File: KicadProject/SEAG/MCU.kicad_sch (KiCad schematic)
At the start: 11 parts, among them IC1 STM32F722RCT6, SW1 SW_SPDT, Y1 Crystal_GND24

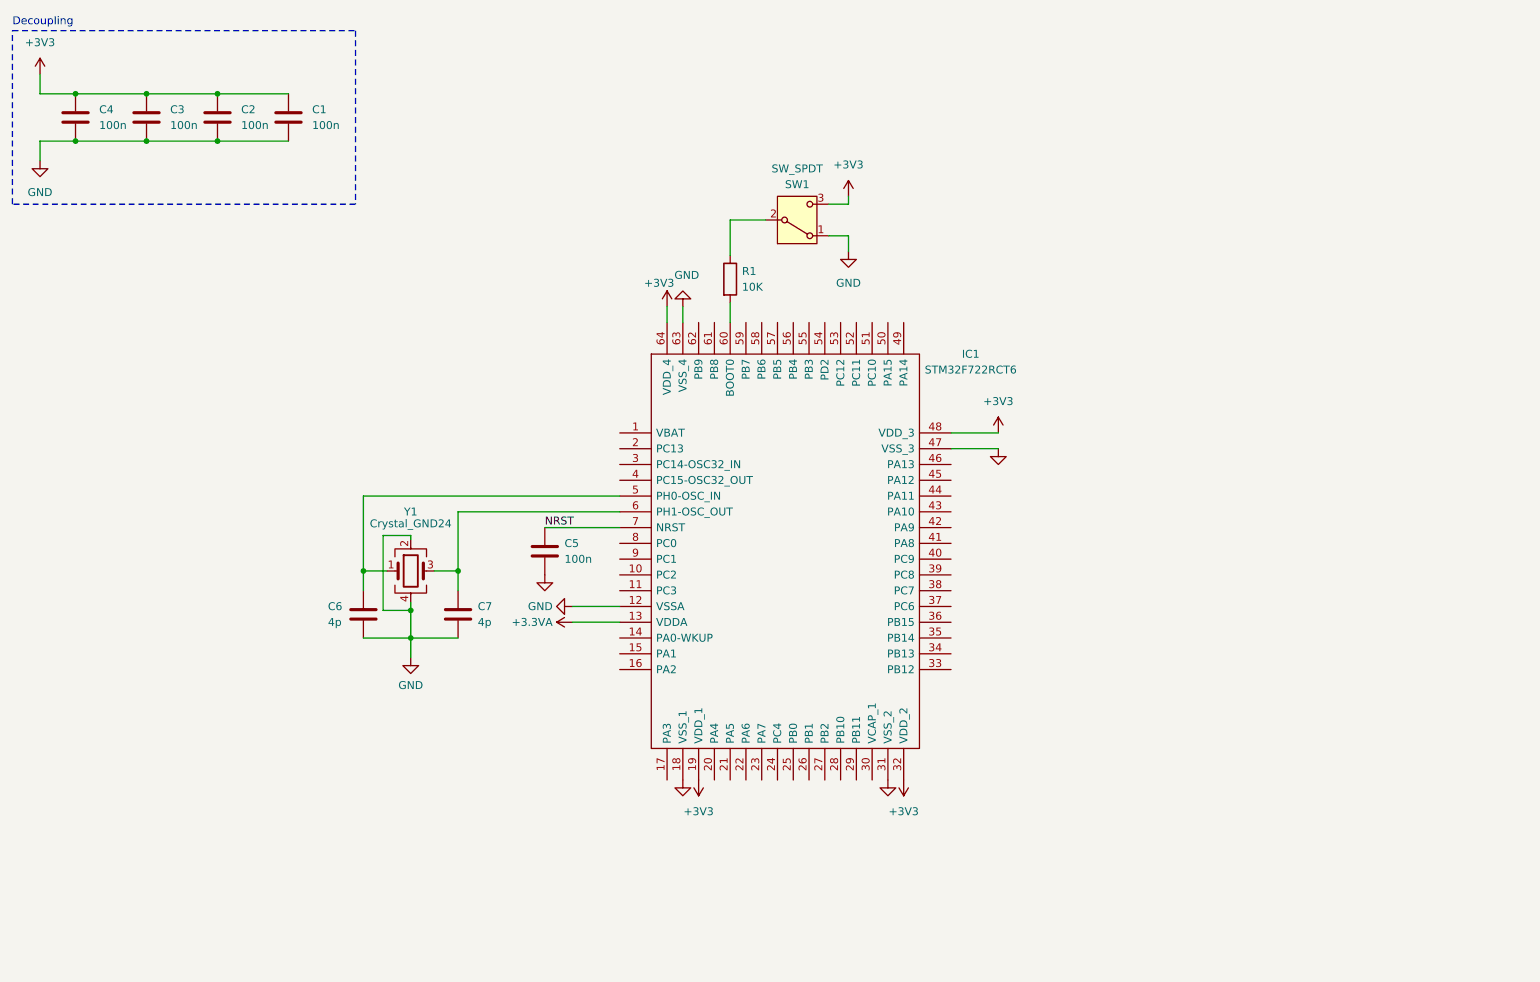
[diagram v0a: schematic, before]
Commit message: Added power supply and serial link header to PCB schematic
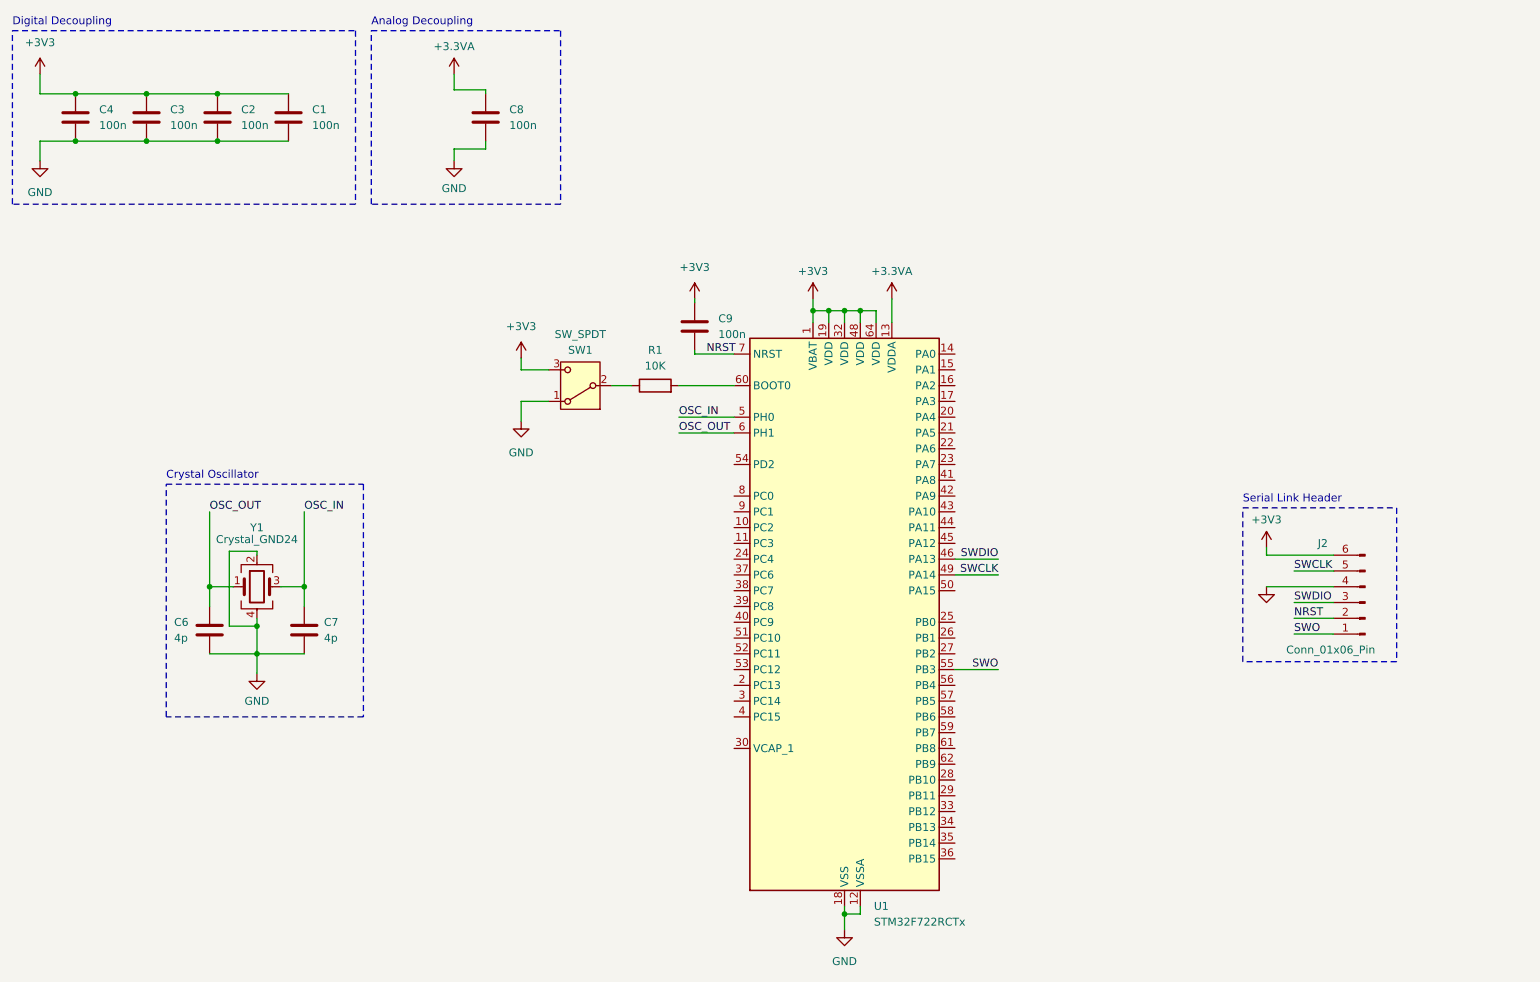
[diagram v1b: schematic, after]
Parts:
- removed C5: 100n, symbol Device:C
- removed IC1: STM32F722RCT6, QFP50P1200X1200X160-64N, symbol SamacSys_Parts:STM32F722RCT6
- added C8, C9: 100n, symbol Device:C
- added J2: Conn_01x06_Pin, Connector_PinHeader_2.54mm:PinHeader_1x06_P2.54mm_Vertical, symbol Connector:Conn_01x06_Pin
- added U1: STM32F722RCTx, Package_QFP:LQFP-64_10x10mm_P0.5mm, symbol MCU_ST_STM32F7:STM32F722RCTx
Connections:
- net +3.3VA: now also C8.1, U1.13 (VDDA)
- net +3V3: now also C9.1, J2.6 (Pin_6), U1.1 (VBAT), U1.19 (VDD), U1.32 (VDD), U1.48 (VDD), U1.64 (VDD)
- net GND: now also C8.2, J2.4 (Pin_4), U1.12 (VSSA), U1.18 (VSS), U1.31 (VSS), U1.47 (VSS), U1.63 (VSS)
- net NRST: now also C9.2, J2.2 (Pin_2), U1.7 (NRST)
- net OSC_IN: now reaches C7.1, Y1.3
- net OSC_IN: now also U1.5 (PH0)
- net at R1.2: now also U1.60 (BOOT0)
- net OSC_OUT: now reaches C6.1, Y1.1
- net OSC_OUT: now also U1.6 (PH1)
- new net SWCLK: J2.5 (Pin_5), U1.49 (PA14)
- new net SWDIO: J2.3 (Pin_3), U1.46 (PA13)
- new net SWO: J2.1 (Pin_1), U1.55 (PB3)
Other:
- note added: "Analog Decoupling"
- note added: "Crystal Oscillator"
- note added: "Digital Decoupling"
- note added: "Serial Link Header"
- note removed: "Decoupling"
- title: (none) -> MCU
- moved on the sheet: C6, C7, R1, SW1, Y1

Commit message: Added 'AudioFiltering' and 'Codec' sheets to PCB schematic, started PCB layout with decouple caps and MCU. The codec in sheet 'Codec' is wrong, placed for testing
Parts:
- C1, C2, C3, C4, C6, C7, C8: footprint (none) -> Capacitor_SMD:C_0805_2012Metric
- C13: renamed from C9; footprint (none) -> Capacitor_SMD:C_0805_2012Metric
- R1: footprint (none) -> Resistor_SMD:R_0805_2012Metric
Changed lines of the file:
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@@
       (effects (font (size 1.27 1.27)) (justify left))
     )
-    (property "Footprint" "" (at 68.9102 120.65 0)
+    (property "Footprint" "Capacitor_SMD:C_0805_2012Metric" (at 68.9102 120.65 0)
       (effects (font (size 1.27 1.27)) hide)
     )
@@
       (effects (font (size 1.27 1.27)) (justify left))
     )
-    (property "Footprint" "" (at 66.3702 38.1 0)
+    (property "Footprint" "Capacitor_SMD:C_0805_2012Metric" (at 66.3702 38.1 0)
       (effects (font (size 1.27 1.27)) hide)
     )
@@
       (effects (font (size 1.27 1.27)))
     )
-    (property "Footprint" "" (at 124.46 79.248 90)
+    (property "Footprint" "Resistor_SMD:R_0805_2012Metric" (at 124.46 79.248 90)
       (effects (font (size 1.27 1.27)) hide)
     )
@@
       (effects (font (size 1.27 1.27)) (justify left))
     )
-    (property "Footprint" "" (at 43.5102 38.1 0)
+    (property "Footprint" "Capacitor_SMD:C_0805_2012Metric" (at 43.5102 38.1 0)
       (effects (font (size 1.27 1.27)) hide)
     )
@@
       (effects (font (size 1.27 1.27)) (justify left))
     )
-    (property "Footprint" "" (at 98.1202 38.1 0)
+    (property "Footprint" "Capacitor_SMD:C_0805_2012Metric" (at 98.1202 38.1 0)
       (effects (font (size 1.27 1.27)) hide)
     )
@@
       (effects (font (size 1.27 1.27)) (justify left))
     )
-    (property "Footprint" "" (at 54.9402 38.1 0)
+    (property "Footprint" "Capacitor_SMD:C_0805_2012Metric" (at 54.9402 38.1 0)
       (effects (font (size 1.27 1.27)) hide)
     )
@@
   (symbol (lib_id "Device:C") (at 130.81 67.945 0) (unit 1)
     (in_bom yes) (on_board yes) (dnp no) (fields_autoplaced)
-    (property "Reference" "C9" (at 134.62 66.675 0)
+    (property "Reference" "C13" (at 134.62 66.675 0)
       (effects (font (size 1.27 1.27)) (justify left))
     )
@@
       (effects (font (size 1.27 1.27)) (justify left))
     )
-    (property "Footprint" "" (at 131.7752 71.755 0)
+    (property "Footprint" "Capacitor_SMD:C_0805_2012Metric" (at 131.7752 71.755 0)
       (effects (font (size 1.27 1.27)) hide)
     )
@@
       (project "SEAG"
         (path "/37e7da6e-dab5-4e62-b28a-754ec4806405/73c774ae-3af2-431c-8167-2f494c9438a8"
-          (reference "C9") (unit 1)
+          (reference "C13") (unit 1)
         )
       )
@@
       (effects (font (size 1.27 1.27)) (justify left))
     )
-    (property "Footprint" "" (at 32.0802 38.1 0)
+    (property "Footprint" "Capacitor_SMD:C_0805_2012Metric" (at 32.0802 38.1 0)
       (effects (font (size 1.27 1.27)) hide)
     )
@@
       (effects (font (size 1.27 1.27)) (justify left))
     )
-    (property "Footprint" "" (at 53.6702 120.65 0)
-      (effects (font (size 1.27 1.27)) hide)
-    )
+    (property "Footprint" "Capacitor_SMD:C_0805_2012Metric" (at 53.6702 120.65 0)
+      (effects (font (size 1.27 1.27)) hide)
+    )

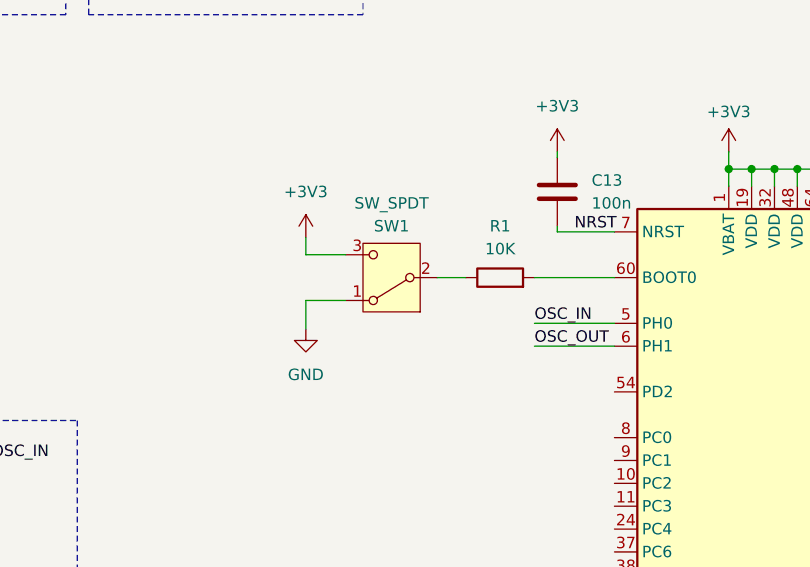
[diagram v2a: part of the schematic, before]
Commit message: Added ESD protection, extra filtering with ferrite bead
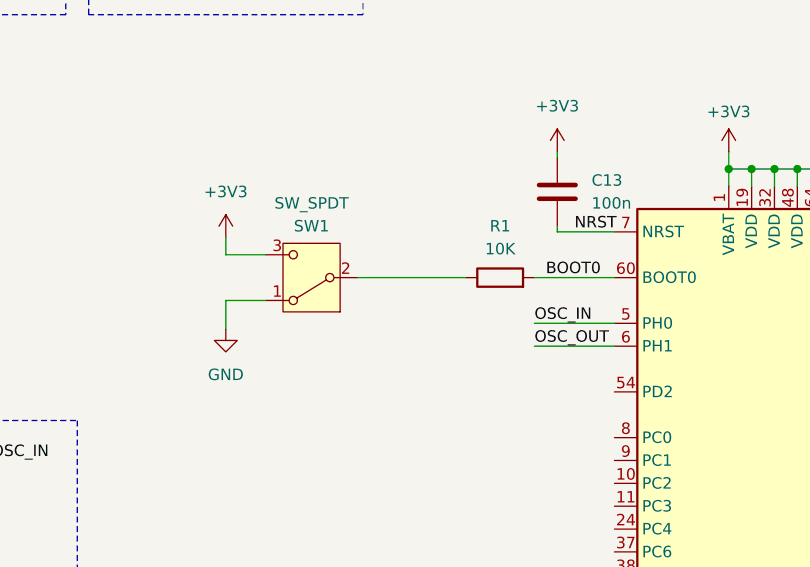
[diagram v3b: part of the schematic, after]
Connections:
- net BOOT0: now reaches R1.2, U1.60 (BOOT0)
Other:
- moved on the sheet: SW1
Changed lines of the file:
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@@
     (stroke (width 0) (type default))
   )
-  (wire (pts (xy 117.475 77.47) (xy 120.65 77.47))
+  (wire (pts (xy 108.585 77.47) (xy 120.65 77.47))
     (stroke (width 0) (type default))
   )
@@
     (stroke (width 0) (type default))
   )
-  (wire (pts (xy 102.87 74.93) (xy 107.315 74.93))
+  (wire (pts (xy 93.98 74.93) (xy 98.425 74.93))
     (stroke (width 0) (type default))
   )
@@
     (stroke (width 0) (type default))
   )
-  (wire (pts (xy 102.87 80.01) (xy 102.87 83.185))
+  (wire (pts (xy 93.98 80.01) (xy 93.98 83.185))
     (stroke (width 0) (type default))
   )
@@
     (stroke (width 0) (type default))
   )
-  (wire (pts (xy 102.87 73.025) (xy 102.87 74.93))
+  (wire (pts (xy 93.98 73.025) (xy 93.98 74.93))
     (stroke (width 0) (type default))
   )
@@
     (stroke (width 0) (type default))
   )
-  (wire (pts (xy 107.315 80.01) (xy 102.87 80.01))
+  (wire (pts (xy 98.425 80.01) (xy 93.98 80.01))
     (stroke (width 0) (type default))
   )
@@
   )
   (label "SWO" (at 227.33 117.475 0) (fields_autoplaced)
+    (effects (font (size 1.27 1.27)) (justify left bottom))
+  )
+  (label "BOOT0" (at 129.54 77.47 0) (fields_autoplaced)
     (effects (font (size 1.27 1.27)) (justify left bottom))
   )
@@
     )
   )
-  (symbol (lib_id "Switch:SW_SPDT") (at 112.395 77.47 180) (unit 1)
+  (symbol (lib_id "Switch:SW_SPDT") (at 103.505 77.47 180) (unit 1)
     (in_bom yes) (on_board yes) (dnp no)
-    (property "Reference" "SW1" (at 112.395 71.755 0)
-      (effects (font (size 1.27 1.27)))
-    )
-    (property "Value" "SW_SPDT" (at 112.395 69.215 0)
-      (effects (font (size 1.27 1.27)))
-    )
-    (property "Footprint" "" (at 112.395 77.47 0)
-      (effects (font (size 1.27 1.27)) hide)
-    )
-    (property "Datasheet" "~" (at 112.395 69.85 0)
+    (property "Reference" "SW1" (at 103.505 71.755 0)
+      (effects (font (size 1.27 1.27)))
+    )
+    (property "Value" "SW_SPDT" (at 103.505 69.215 0)
+      (effects (font (size 1.27 1.27)))
+    )
+    (property "Footprint" "" (at 103.505 77.47 0)
+      (effects (font (size 1.27 1.27)) hide)
+    )
+    (property "Datasheet" "~" (at 103.505 69.85 0)
       (effects (font (size 1.27 1.27)) hide)
     )
@@
     )
   )
-  (symbol (lib_id "power:GND") (at 102.87 83.185 0) (unit 1)
-    (in_bom yes) (on_board yes) (dnp no) (fields_autoplaced)
-    (property "Reference" "#PWR01" (at 102.87 89.535 0)
-      (effects (font (size 1.27 1.27)) hide)
-    )
-    (property "Value" "GND" (at 102.87 88.265 0)
-      (effects (font (size 1.27 1.27)))
-    )
-    (property "Footprint" "" (at 102.87 83.185 0)
-      (effects (font (size 1.27 1.27)) hide)
-    )
-    (property "Datasheet" "" (at 102.87 83.185 0)
+  (symbol (lib_id "power:GND") (at 93.98 83.185 0) (unit 1)
+    (in_bom yes) (on_board yes) (dnp no) (fields_autoplaced)
+    (property "Reference" "#PWR01" (at 93.98 89.535 0)
+      (effects (font (size 1.27 1.27)) hide)
+    )
+    (property "Value" "GND" (at 93.98 88.265 0)
+      (effects (font (size 1.27 1.27)))
+    )
+    (property "Footprint" "" (at 93.98 83.185 0)
+      (effects (font (size 1.27 1.27)) hide)
+    )
+    (property "Datasheet" "" (at 93.98 83.185 0)
       (effects (font (size 1.27 1.27)) hide)
     )
@@
     )
   )
-  (symbol (lib_id "power:+3V3") (at 102.87 73.025 0) (unit 1)
-    (in_bom yes) (on_board yes) (dnp no) (fields_autoplaced)
-    (property "Reference" "#PWR02" (at 102.87 76.835 0)
-      (effects (font (size 1.27 1.27)) hide)
-    )
-    (property "Value" "+3V3" (at 102.87 67.945 0)
-      (effects (font (size 1.27 1.27)))
-    )
-    (property "Footprint" "" (at 102.87 73.025 0)
-      (effects (font (size 1.27 1.27)) hide)
-    )
-    (property "Datasheet" "" (at 102.87 73.025 0)
-      (effects (font (size 1.27 1.27)) hide)
-    )
+  (symbol (lib_id "power:+3V3") (at 93.98 73.025 0) (unit 1)
+    (in_bom yes) (on_board yes) (dnp no) (fields_autoplaced)
+    (property "Reference" "#PWR02" (at 93.98 76.835 0)
+      (effects (font (size 1.27 1.27)) hide)
+    )
+    (property "Value" "+3V3" (at 93.98 67.945 0)
+      (effects (font (size 1.27 1.27)))
+    )
+    (property "Footprint" "" (at 93.98 73.025 0)
+      (effects (font (size 1.27 1.27)) hide)
+    )
+    (property "Datasheet" "" (at 93.98 73.025 0)
+      (effects (font (size 1.27 1.27)) hide)
+    )
